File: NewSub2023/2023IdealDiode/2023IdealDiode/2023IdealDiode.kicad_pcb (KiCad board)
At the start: 2 copper layers, 80.6 x 61 mm, 12 parts, among them J1 Battery 1 Input, J2 Battery 2 Input, J3 Output, Q1 NMOS, Q2 NMOS, SW1 Power Switch

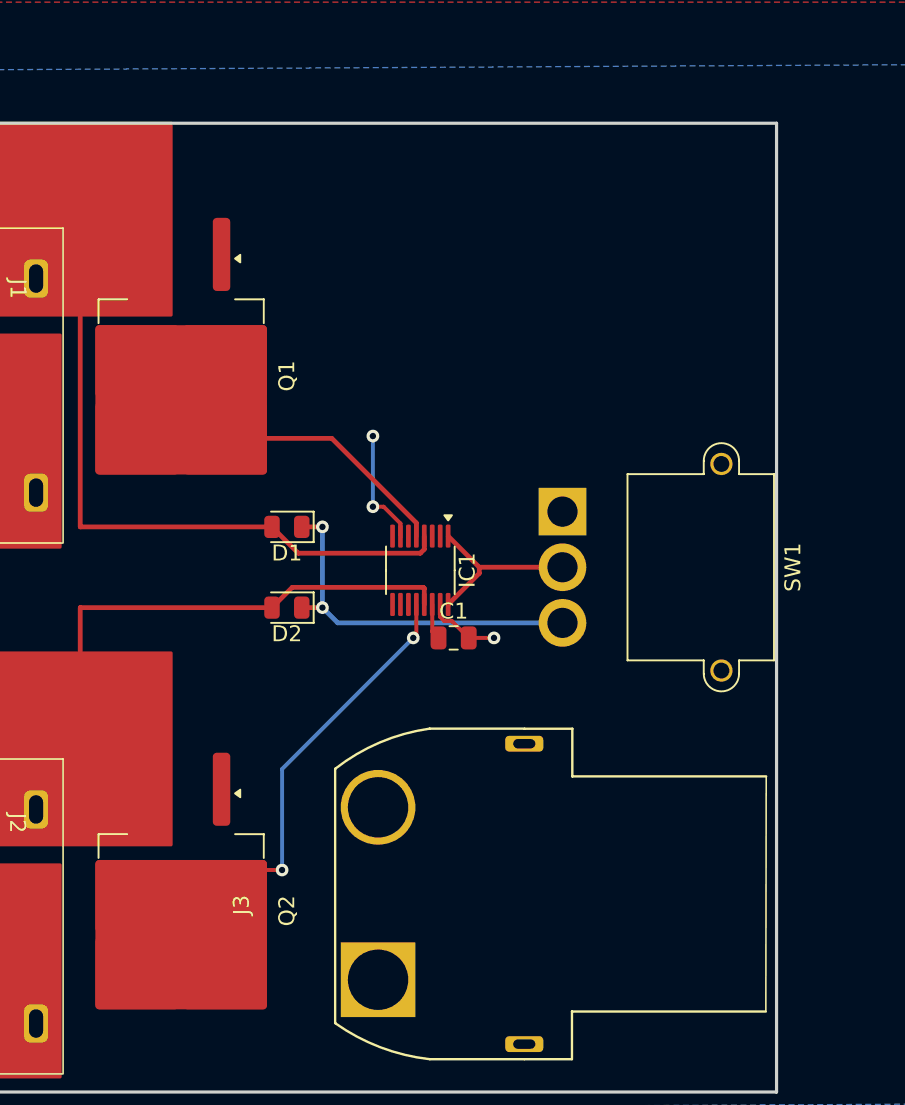
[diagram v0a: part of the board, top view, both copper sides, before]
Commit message: Created Gerber Files for Ideal 2023IdealDiode
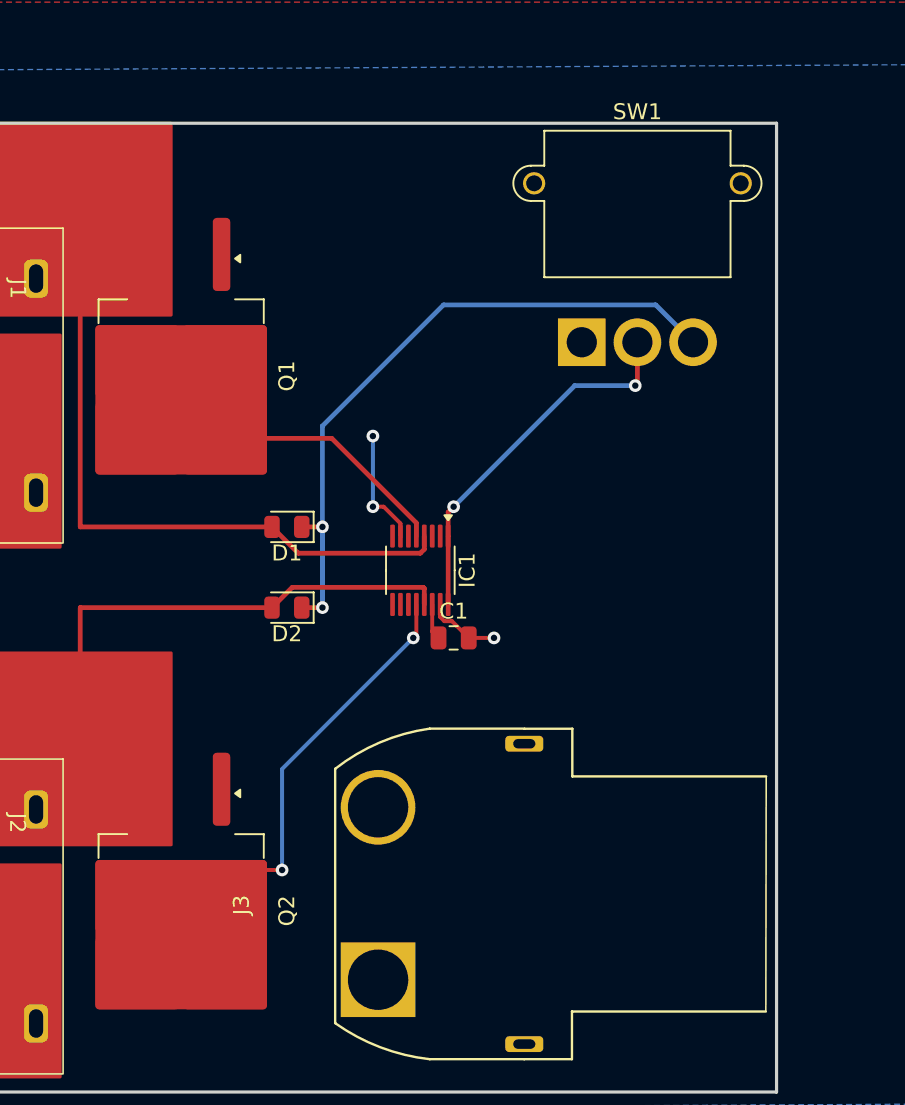
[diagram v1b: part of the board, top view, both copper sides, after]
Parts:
- moved SW1 10.7 mm to (347.2, 235.4), turned to 0 degrees
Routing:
- net Net-(D1-K): track 23.2 -> 46.6 mm
- net Net-(IC1-EN1): track 11.2 -> 23.7 mm, vias 0 -> 2

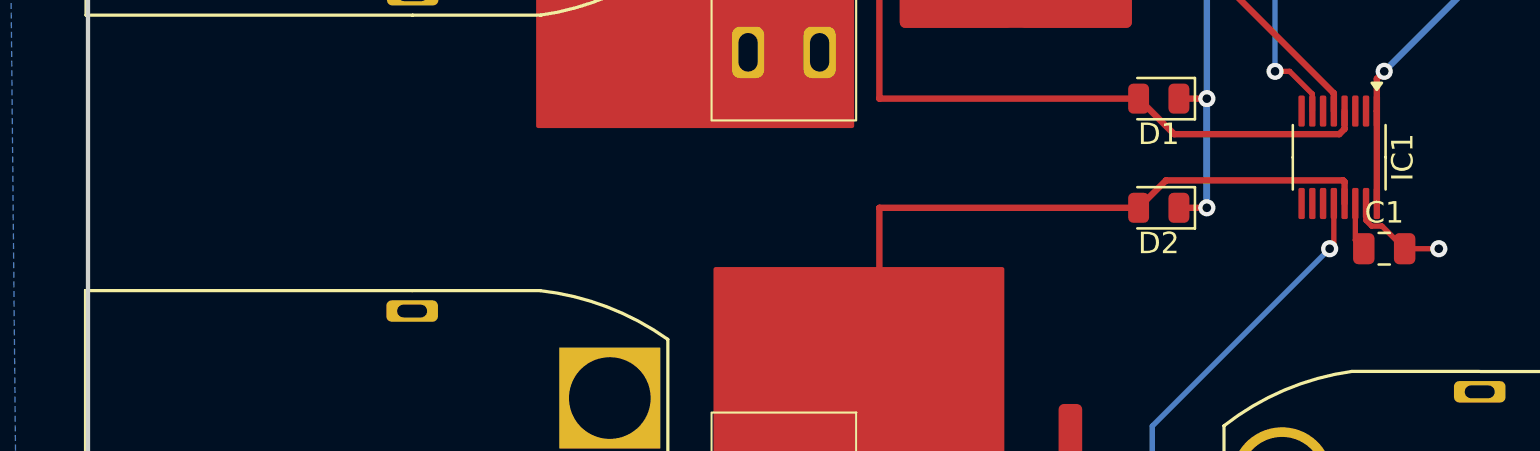
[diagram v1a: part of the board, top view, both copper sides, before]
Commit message: Finished and created gerber files for ideal diode pcb
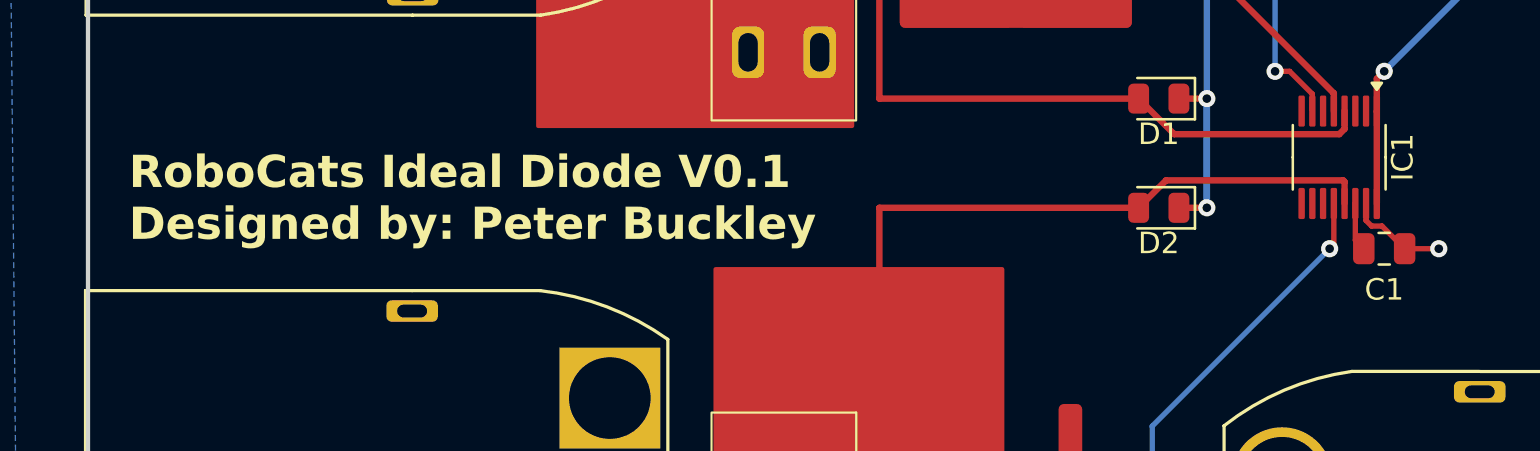
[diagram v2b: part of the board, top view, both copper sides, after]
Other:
- board text added: "RoboCats Ideal Diode V0.1 Designed by: Peter Buckley"
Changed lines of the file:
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@@
 			(outputformat 1)
 			(mirror no)
-			(drillshape 1)
+			(drillshape 0)
 			(scaleselection 1)
-			(outputdirectory "")
+			(outputdirectory "GerberFiles/")
 		)
 	)
@@
 		(tags "capacitor")
 		(property "Reference" "C1"
-			(at 0 -1.68 0)
+			(at 0 1.905 0)
 			(layer "F.SilkS")
 			(effects
@@
 		)
 		(property "Value" "1uF"
-			(at 0 1.68 0)
+			(at 0 3.175 0)
 			(layer "F.Fab")
 			(effects
@@
 		(layer "Edge.Cuts")
 	)
+	(gr_text "RoboCats Ideal Diode V0.1\nDesigned by: Peter Buckley"
+		(at 280.67 249.555 0)
+		(layer "F.SilkS")
+		(effects
+			(font
+				(size 1.5 1.5)
+				(thickness 0.3)
+				(bold yes)
+			)
+			(justify left top)
+		)
+	)
 	(segment
